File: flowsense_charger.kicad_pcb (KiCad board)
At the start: 2 copper layers, 65.1 x 30 mm, 34 parts, among them J1 SOLAR, J2 LOAD, J3 Conn_01x02_Pin, J4 Conn_02x20_Odd_Even, J5 USB_A, SW1 SW_Push, U1 BQ25185, U2 TPS61230DRC

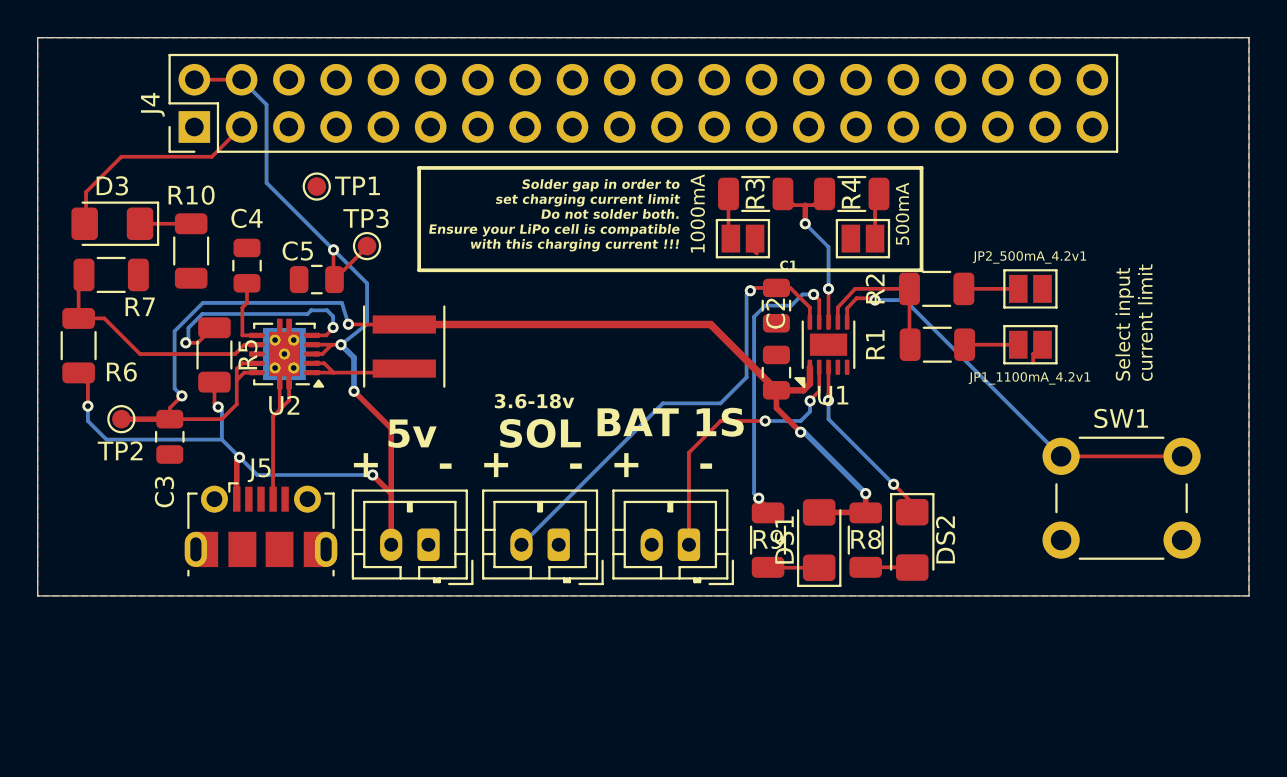
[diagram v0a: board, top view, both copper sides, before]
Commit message: Scheme: Fixes capacitor issue on PIN1 SYS of U1. Adds decoupler 1uF on PIN2 BAT of U1. Clarifies text
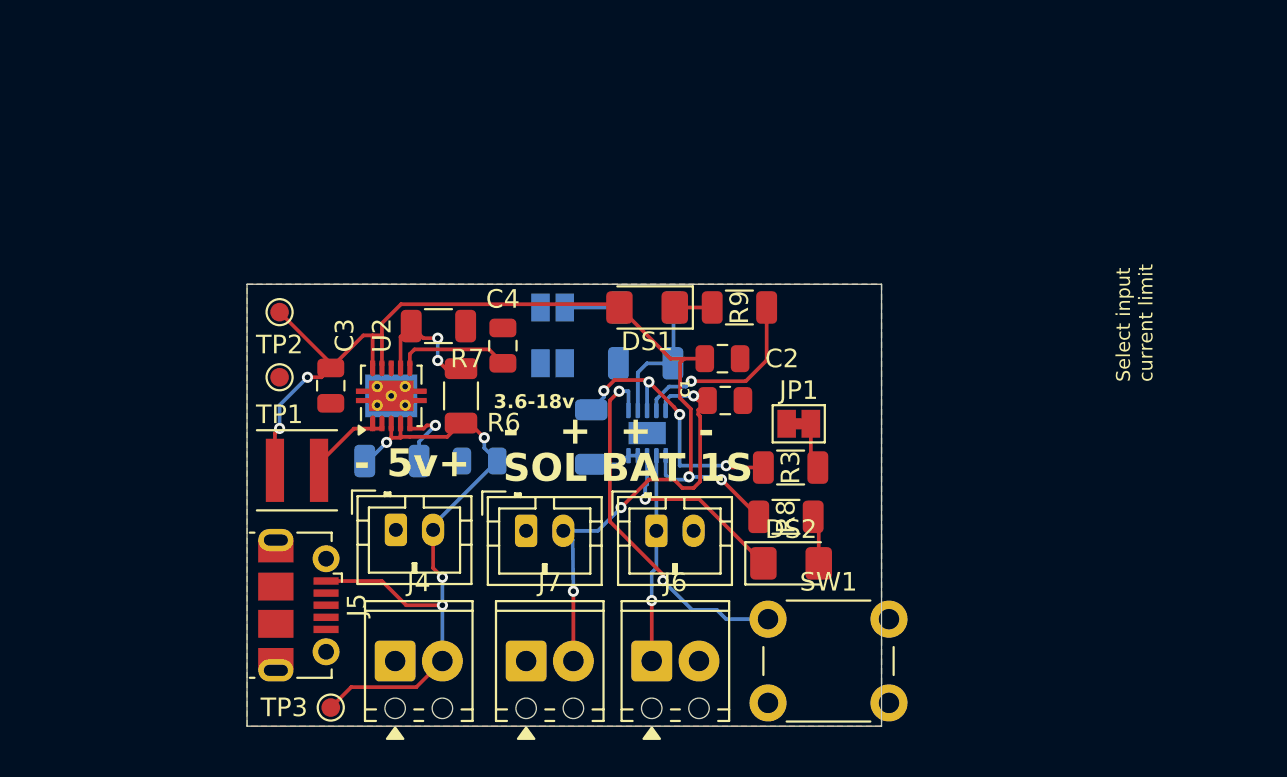
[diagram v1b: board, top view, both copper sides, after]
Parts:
- removed 1000mA, 500mA: SolderJumper_2_Open, Jumper:SolderJumper-2_P1.3mm_Open_Pad1.0x1.5mm
- removed D3: LED, LED_SMD:LED_1206_3216Metric_Pad1.42x1.75mm_HandSolder
- removed R10: 470, Resistor_SMD:R_1206_3216Metric
- removed R4: 600 ohm, Resistor_SMD:R_1206_3216Metric
- added J6: Conn_01x02_Pin, TerminalBlock_Phoenix:TerminalBlock_Phoenix_MPT-0,5-2-2.54_1x02_P2.54mm_Horizontal, F.Cu at (47.5, 94.5)
- added J7: SOLAR, TerminalBlock_Phoenix:TerminalBlock_Phoenix_MPT-0,5-2-2.54_1x02_P2.54mm_Horizontal, F.Cu at (40.8, 94.5)
- added JP1: SJ2, Jumper:SolderJumper-2_P1.3mm_Bridged_Pad1.0x1.5mm, F.Cu at (55.4, 81.8)
- added R11: 600 ohm, Resistor_SMD:R_1206_3216Metric, B.Cu at (44.2, 82.5)
- C5, JP1_1100mA_4.2v1, JP2_500mA_4.2v1, R1, R2, R5, U1: moved to B.Cu
- J4: value Conn_02x20_Odd_Even -> LOAD; footprint Connector_PinHeader_2.54mm:PinHeader_2x20_P2.54mm_Vertical -> TerminalBlock_Phoenix:TerminalBlock_Phoenix_MPT-0,5-2-2.54_1x02_P2.54mm_Horizontal
- R3: value 300 ohm -> 600 ohm
- moved J4 30.7 mm to (33.7, 94.5), turned to 0 degrees
- moved JP1_1100mA_4.2v1 25.7 mm to (42.2, 78.5), turned to 0 degrees
- moved JP2_500mA_4.2v1 25.7 mm to (42.2, 75.5), turned to 0 degrees
- moved TP3 24.9 mm to (30.2, 97.0), turned to 90 degrees
- moved R6 20.7 mm to (37.2, 80.2)
- moved SW1 18.0 mm to (53.8, 92.2)
- moved R7 17.8 mm to (36.0, 76.5)
- moved R1 15.7 mm to (47.2, 78.5), turned to 180 degrees
- moved R2 15.6 mm to (47.2, 75.5), turned to 180 degrees
- moved DS1 15.6 mm to (47.2, 75.5), turned to 180 degrees
- moved R3 14.8 mm to (55.0, 84.1), turned to 0 degrees
- moved C4 14.4 mm to (39.5, 77.5)
- moved C5 13.1 mm to (38.2, 83.8)
- moved R9 12.6 mm to (52.2, 75.5), turned to 0 degrees
- moved R5 11.1 mm to (33.5, 83.8), turned to 180 degrees
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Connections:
- J4 pad 1: unconnected-(J4-Pin_1-Pad1) -> GND
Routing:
- net +5V: track 64.8 -> 36.6 mm, vias 7 -> 4
- net V_SYS: track 64.9 -> 51.5 mm
- net Net-(D3-A): track 11.3 -> 0.00 mm
- net Net-(U2-PG): track 13.0 -> 3.72 mm, vias 2 -> 1
- net GND: track 9.96 -> 2.69 mm
- net Net-(U2-FB): track 12.9 -> 6.84 mm, vias 0 -> 2
- net Net-(U1-STAT1): track 16.2 -> 10.2 mm, vias 2 -> 1
- net ISET: track 9.54 -> 15.3 mm, vias 2 -> 4
- net +BATT: track 15.0 -> 11.5 mm, vias 2 -> 1
- net Net-(D3-K): track 2.95 -> 0.00 mm
- net Net-(JP1_1100mA_4.2v1-B): track 2.89 -> 0.00 mm
- net Net-(U1-TS/MR): track 22.5 -> 19.6 mm, vias 1 -> 2
- net Net-(U2-SS): track 3.40 -> 5.90 mm
- net Net-(JP4_ISET_500mA1-B): track 2.49 -> 0.00 mm
- net Net-(J1-Pin_2): track 25.0 -> 23.6 mm, vias 1 -> 3
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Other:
- board size 65.1 x 30 mm -> 34.1 x 23.8 mm
- board text added: "Solder gap to set charging current limit Do not solder both. Ensure your cell is compatible with charging current !"
- board text removed: "Solder gap in order to set charging current limit Do not solder both. Ensure your LiPo cell is compatible with this charging current !!!"

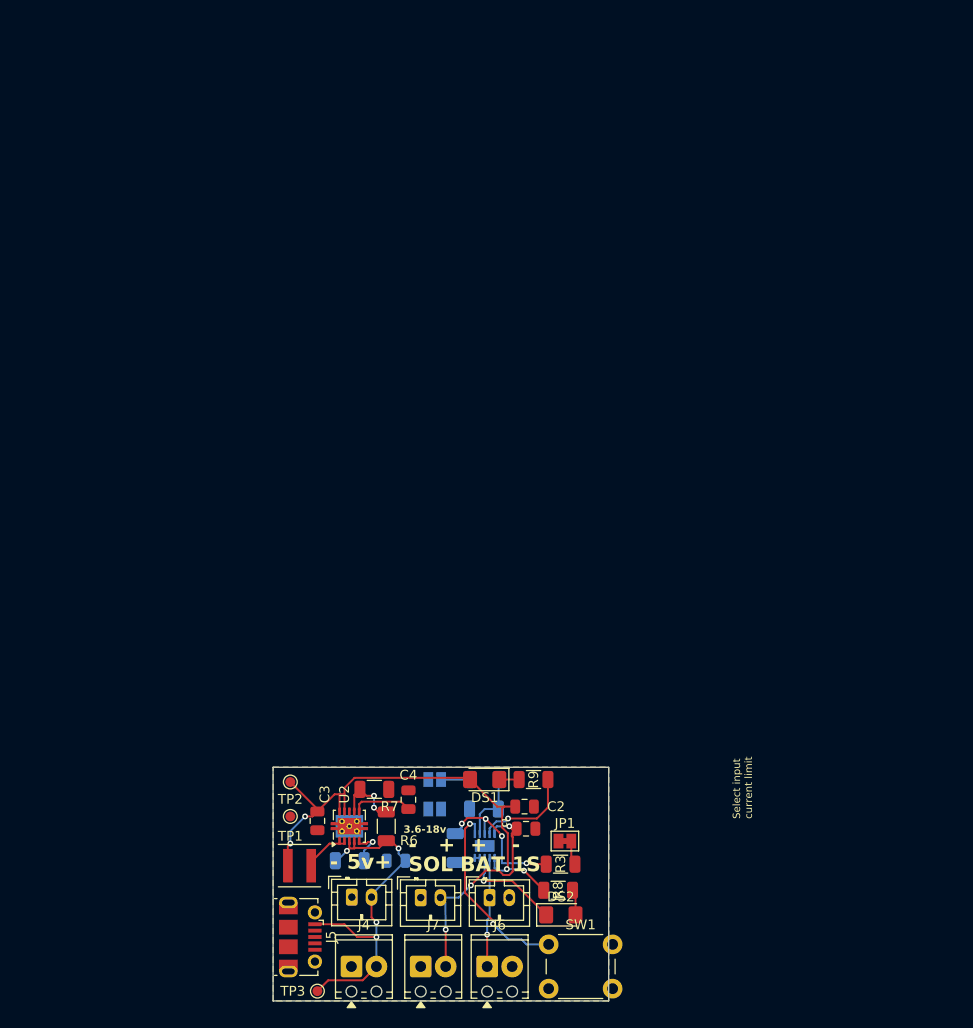
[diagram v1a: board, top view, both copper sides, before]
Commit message: Starts implementing non-regulated output, and alternative 3.3v regulated output.
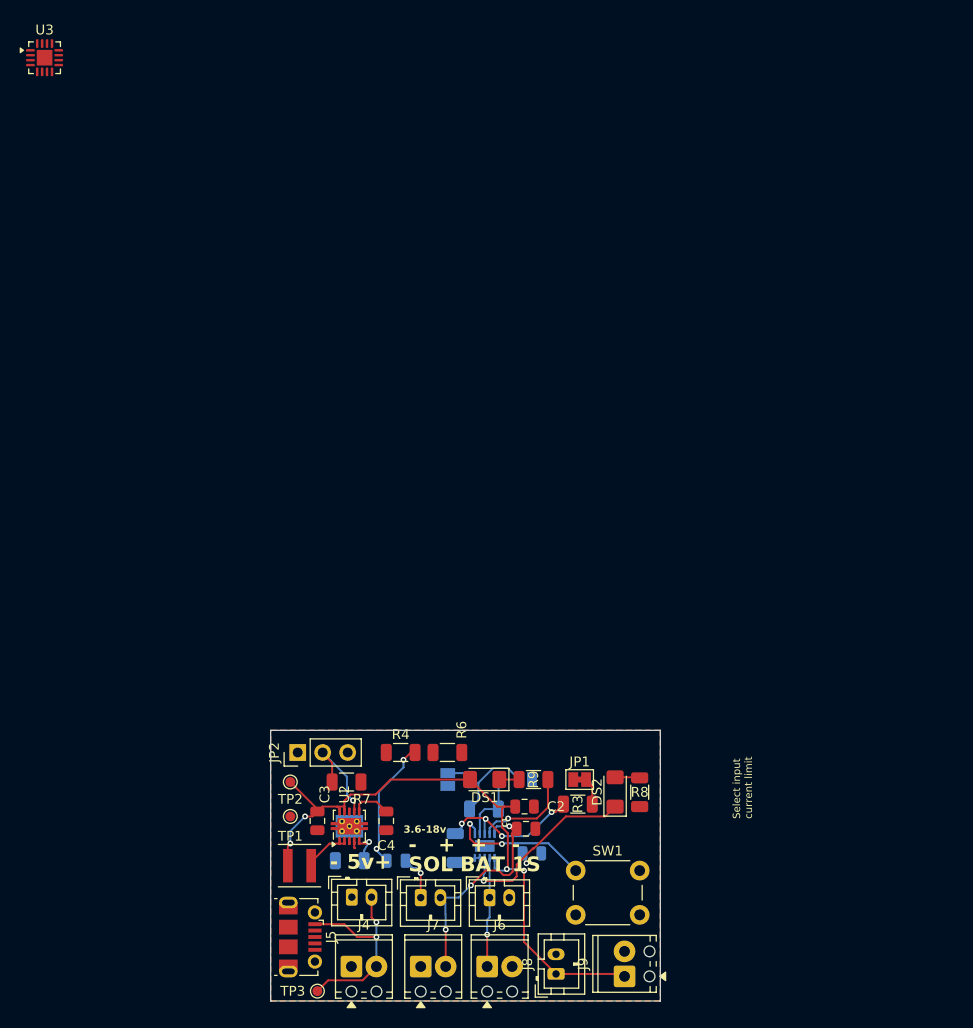
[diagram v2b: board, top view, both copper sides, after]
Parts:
- added C6: 1uF, Capacitor_SMD:C_0805_2012Metric, B.Cu at (52.0, 83.0)
- added J8: Conn_01x02_Pin, Connector_JST:JST_PH_B2B-PH-K_1x02_P2.00mm_Vertical, F.Cu at (54.5, 95.2)
- added J9: Conn_01x02_Pin, TerminalBlock_Phoenix:TerminalBlock_Phoenix_MPT-0,5-2-2.54_1x02_P2.54mm_Horizontal, F.Cu at (61.5, 95.5)
- added JP2: Jumper_3_Bridged12, Connector_PinHeader_2.54mm:PinHeader_1x03_P2.54mm_Vertical, F.Cu at (28.2, 72.8)
- added R4: 230K, Resistor_SMD:R_1206_3216Metric, F.Cu at (38.7, 72.8)
- added U3: BQ24074RGT, Package_DFN_QFN:VQFN-16-1EP_3x3mm_P0.5mm_EP1.6x1.6mm, F.Cu at (2.53, 2.15)
- C2: value 1uF -> 10uF
- moved DS2 13.7 mm to (60.5, 76.8), turned to 90 degrees
- moved R8 13.0 mm to (63.0, 76.8), turned to -90 degrees
- moved R6 9.74 mm to (43.5, 72.8), turned to 180 degrees
- moved JP1_1100mA_4.2v1 9.70 mm to (51.4, 75.5), turned to 180 degrees
- moved SW1 7.99 mm to (56.5, 84.8)
- moved JP1 6.43 mm to (56.9, 75.5)
- moved R3 6.35 mm to (56.7, 78.0)
- moved C4 3.11 mm to (37.2, 79.7), turned to -90 degrees
- moved R7 2.92 mm to (33.2, 75.8)
- moved JP2_500mA_4.2v1 1.33 mm to (43.5, 75.5), turned to 90 degrees
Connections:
- C5 pad 1: +5V -> GND
- C5 pad 2: GND -> VCC
- J2 pad 2: +5V -> VCC
- J4 pad 2: +5V -> VCC
- R5 pad 2: +5V -> VOUT
- R6 pad 1: +5V -> VCC
- R6 pad 2: Net-(U2-FB) -> Net-(JP2-A)
- R7 pad 1: Net-(U2-FB) -> SET_V
- U2 pad 3: +5V -> VCC
- U2 pad 4: +5V -> VCC
- U2 pad 7: Net-(U2-FB) -> SET_V
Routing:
- net +5V: track 36.6 -> 21.3 mm, vias 4 -> 2
- net VCC: track 0.00 -> 14.2 mm, vias 0 -> 2
- net V_SYS: track 51.5 -> 64.7 mm
- net SET_V: track 0.00 -> 10.5 mm, vias 0 -> 1
- net Net-(DS2-K): track 10.2 -> 19.6 mm
- net Net-(JP1_1100mA_4.2v1-B): track 0.00 -> 8.29 mm
- net Net-(U2-FB): track 6.84 -> 0.00 mm, vias 2 -> 0
- net Net-(U1-TS/MR): track 19.6 -> 14.9 mm
- net GND: track 2.69 -> 6.86 mm, vias 0 -> 1
- net Net-(U2-SS): track 5.90 -> 3.76 mm
- net Net-(U2-PG): track 3.72 -> 3.12 mm
- net +BATT: track 11.5 -> 11.6 mm, vias 1 -> 2
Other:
- board size 34.1 x 23.8 mm -> 39.6 x 27.5 mm

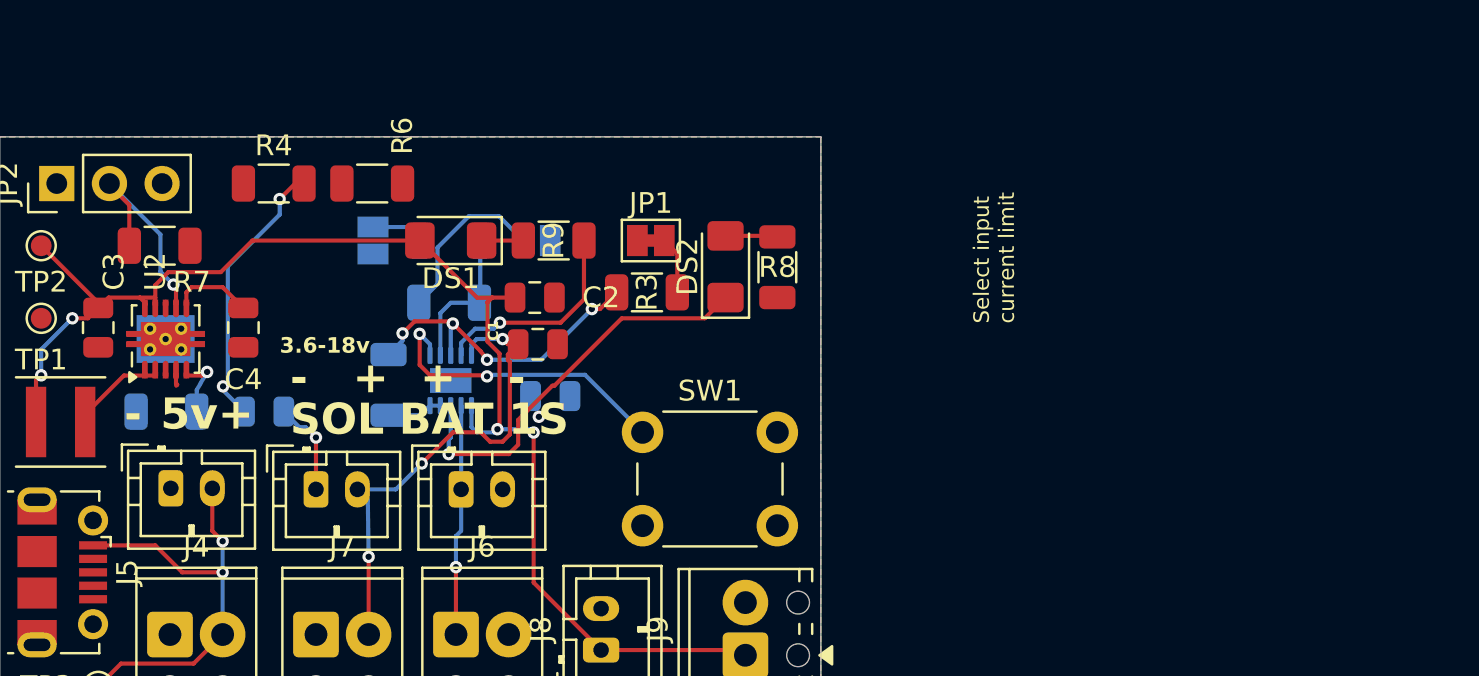
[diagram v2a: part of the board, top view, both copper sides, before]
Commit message: Rearrange text on schematic a bit
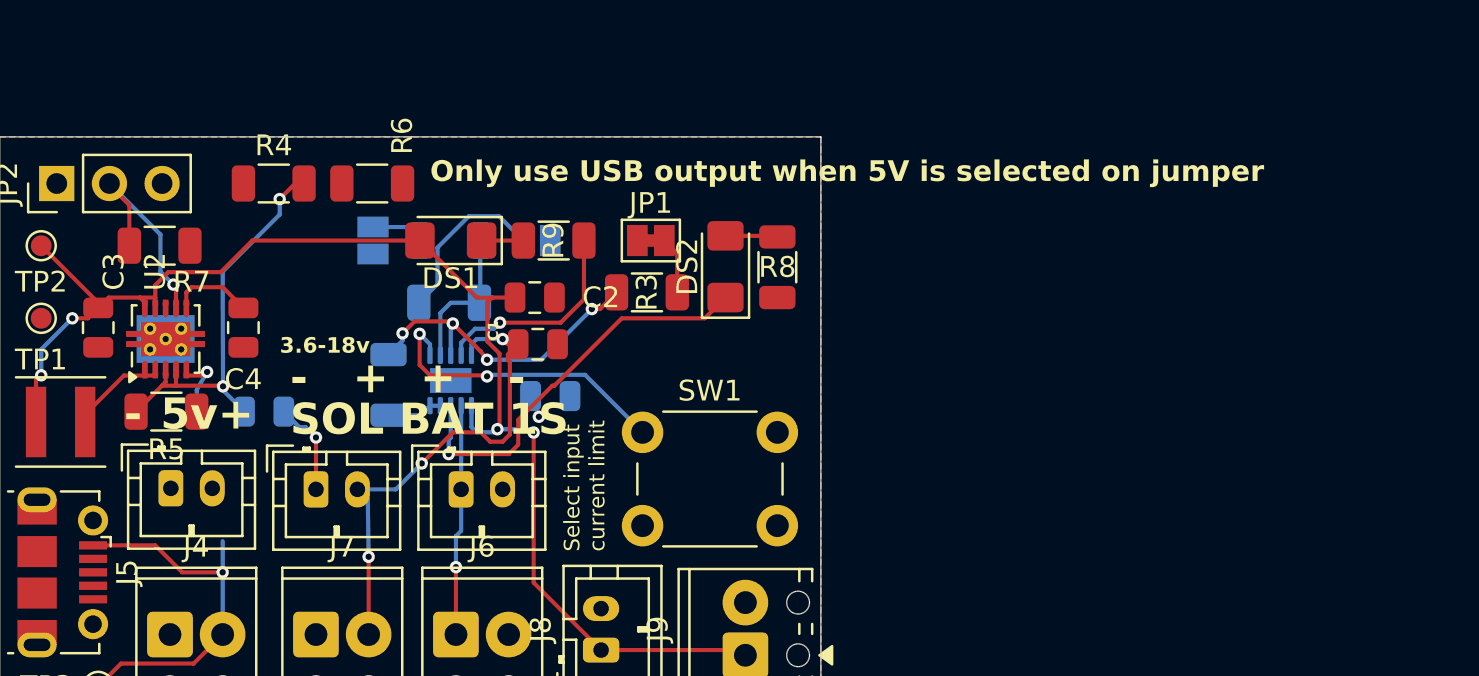
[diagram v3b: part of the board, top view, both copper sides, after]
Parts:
- R5: moved to F.Cu
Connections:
- J5 pad 1: +5V -> VOUT
- R5 pad 2: VOUT -> VCC
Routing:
- net VCC: track 14.2 -> 19.3 mm
- net +5V: track 21.3 -> 18.3 mm, vias 2 -> 1
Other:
- board text added: "Only use USB output when 5V is selected on jumper"
